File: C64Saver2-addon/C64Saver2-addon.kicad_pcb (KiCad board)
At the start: 2 copper layers, 45.7 x 35.6 mm, 25 parts, among them J1 Conn_01x12_Female, J2 Conn_01x07_Female, J3 OLED_128x32_Conn_01x04_Male, SW1 SW_Push, SW2 SW_Push, U1 INA219xIDR-SOIC, U2 ISO1541D, U3 ProMicro, U4 4N25, U5 4N25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

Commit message: revision on addon board
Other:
- board text added: "Rev 2.0"
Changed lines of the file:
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@@
     (links 78)
     (no_connects 0)
-    (area 128.06357 76.024761 194.54 122.095239)
+    (area 138.354999 81.204999 184.225001 116.915001)
     (thickness 1.6)
-    (drawings 7)
+    (drawings 9)
     (tracks 372)
     (zones 0)
@@
     (descr "Through hole straight pin header, 1x12, 2.54mm pitch, single row")
     (tags "Through hole pin header THT 1x12 2.54mm single row")
-    (fp_text reference J1 (at 0 30.48 180) (layer F.SilkS)
+    (fp_text reference J1 (at -2.0828 4.8768 180) (layer F.SilkS)
       (effects (font (size 1 1) (thickness 0.15)))
     )
@@
     )
   )
+  (gr_text "Rev 2.0" (at 180.721 84.0232) (layer F.SilkS)
+    (effects (font (size 1.1 1.1) (thickness 0.275)))
+  )
+  (gr_text "C64 Saver\nAddon\nBWACK 2018" (at 175.4378 109.4486) (layer B.SilkS)
+    (effects (font (size 1.25 1.25) (thickness 0.3)) (justify mirror))
+  )
   (gr_text OLED (at 140.335 87.63 90) (layer F.SilkS)

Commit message: saver 2.0beta - addon 1.0beta
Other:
- board text added: "Rev 2.0beta"
- board text removed: "Rev 2.0"
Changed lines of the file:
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@@
     (links 78)
     (no_connects 0)
-    (area 138.354999 81.204999 184.225001 116.915001)
+    (area 128.06357 76.024761 194.54 122.095239)
     (thickness 1.6)
     (drawings 9)
@@
     )
   )
-  (gr_text "Rev 2.0" (at 180.721 84.0232) (layer F.SilkS)
+  (gr_text "Rev 2.0beta" (at 175.26 106.68) (layer F.SilkS)
     (effects (font (size 1.1 1.1) (thickness 0.275)))
   )

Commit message: eddited schematic of addon board
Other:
- board text added: "C64 Saver Addon 1.0 BWACK 2018"
- board text removed: "Rev 2.0beta"
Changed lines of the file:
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@@
     (area 128.06357 76.024761 194.54 122.095239)
     (thickness 1.6)
-    (drawings 9)
+    (drawings 8)
     (tracks 372)
     (zones 0)
@@
     )
   )
-  (gr_text "Rev 2.0beta" (at 175.26 106.68) (layer F.SilkS)
-    (effects (font (size 1.1 1.1) (thickness 0.275)))
-  )
-  (gr_text "C64 Saver\nAddon\nBWACK 2018" (at 175.4378 109.4486) (layer B.SilkS)
+  (gr_text "C64 Saver\nAddon 1.0\nBWACK 2018" (at 175.4378 109.4486) (layer B.SilkS)
     (effects (font (size 1.25 1.25) (thickness 0.3)) (justify mirror))
   )

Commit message: SOP4 model
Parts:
- added R10: 560, Resistors_SMD:R_0603_HandSoldering, F.Cu at (178.0, 106.7)
- added R11: 560, Resistors_SMD:R_0603_HandSoldering, F.Cu at (178.0, 110.5)
- added R9: 560, Resistors_SMD:R_0603_HandSoldering, F.Cu at (172.9, 106.7)
- added U7: AP1117-50, TO_SOT_Packages_SMD:SOT-223-3_TabPin2, F.Cu at (159.0, 98.8)
- D1: footprint Diodes_SMD:D_1206 -> Diodes_SMD:D_SOD-123
- R2: footprint Resistors_SMD:R_2816_HandSoldering -> Resistors_SMD:R_2010_HandSoldering
- moved C1 21.6 mm to (163.1, 106.7), turned to 180 degrees
- moved R1 11.6 mm to (172.9, 93.3)
- moved D1 7.65 mm to (141.3, 114.3)
- moved U4 7.44 mm to (157.7, 92.4)
- moved U5 7.10 mm to (162.7, 92.4)
- moved SW2 5.72 mm to (147.3, 110.5)
- moved SW1 5.56 mm to (157.6, 110.5)
- moved R3 3.07 mm to (153.7, 92.5), turned to 270 degrees
- moved R2 1.91 mm to (158.5, 87.6)
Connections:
- C1 pad 1: 9VAC2 -> GND
- C1 pad 2: /9VRAW -> Net-(C1-Pad2)
- C4 pad 2: +5V -> Net-(C4-Pad2)
- C5 pad 1: Net-(C5-Pad1) -> /9VAC1+
- C5 pad 2: /SENSE_VAC -> Net-(C5-Pad2)
- D1 pad 1: /9VRAW -> Net-(C1-Pad2)
- D1 pad 2: /9VAC1- -> /9VAC1+
- J1 pad 1: /VIN+ -> GND2
- J2 pad 1: GND2 -> /9VAC1+
- J2 pad 2: GND2 -> /9VAC1+
- J2 pad 3: /9VAC1+ -> /9VAC1-
- J2 pad 5: 9VAC2 -> GND
- R7 pad 1: GND -> /SDA2
- R7 pad 2: Net-(C5-Pad1) -> Net-(R7-Pad2)
- R8 pad 1: Net-(C5-Pad1) -> /SENSE_VAC
- R8 pad 2: /9VAC1- -> Net-(C5-Pad2)
- U1 pad 3: /SDA2 -> /SCL2
- U1 pad 4: /SCL2 -> /SDA2
- U3 pad 23: 9VAC2 -> GND
- U3 pad 24: /9VRAW -> (no net)
- U6 pad 8: +5V -> Net-(C4-Pad2)
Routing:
- net GND: track 113.5 -> 0.00 mm
- net +5V: track 77.6 -> 0.00 mm, vias 2 -> 0
- net VIN-: track 59.5 -> 0.00 mm, vias 2 -> 0
- net /SDA1: track 56.4 -> 0.00 mm, vias 1 -> 0
- net GND2: track 55.8 -> 0.00 mm
- net /9VAC1-: track 54.2 -> 0.00 mm, vias 2 -> 0
- net /SCL1: track 47.0 -> 0.00 mm, vias 2 -> 0
- net Net-(C3-Pad2): track 44.1 -> 0.00 mm
- net /VIN+: track 43.8 -> 0.00 mm
- net Net-(SW2-Pad2): track 40.3 -> 0.00 mm
- net /9VRAW: track 38.0 -> 0.00 mm, vias 1 -> 0
- net Net-(SW1-Pad2): track 29.1 -> 0.00 mm
- net 9VAC2: track 27.7 -> 0.00 mm
- net /9VAC1+: track 23.6 -> 0.00 mm, vias 1 -> 0
- net /SENSE_ACCUR: track 20.7 -> 0.00 mm, vias 1 -> 0
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
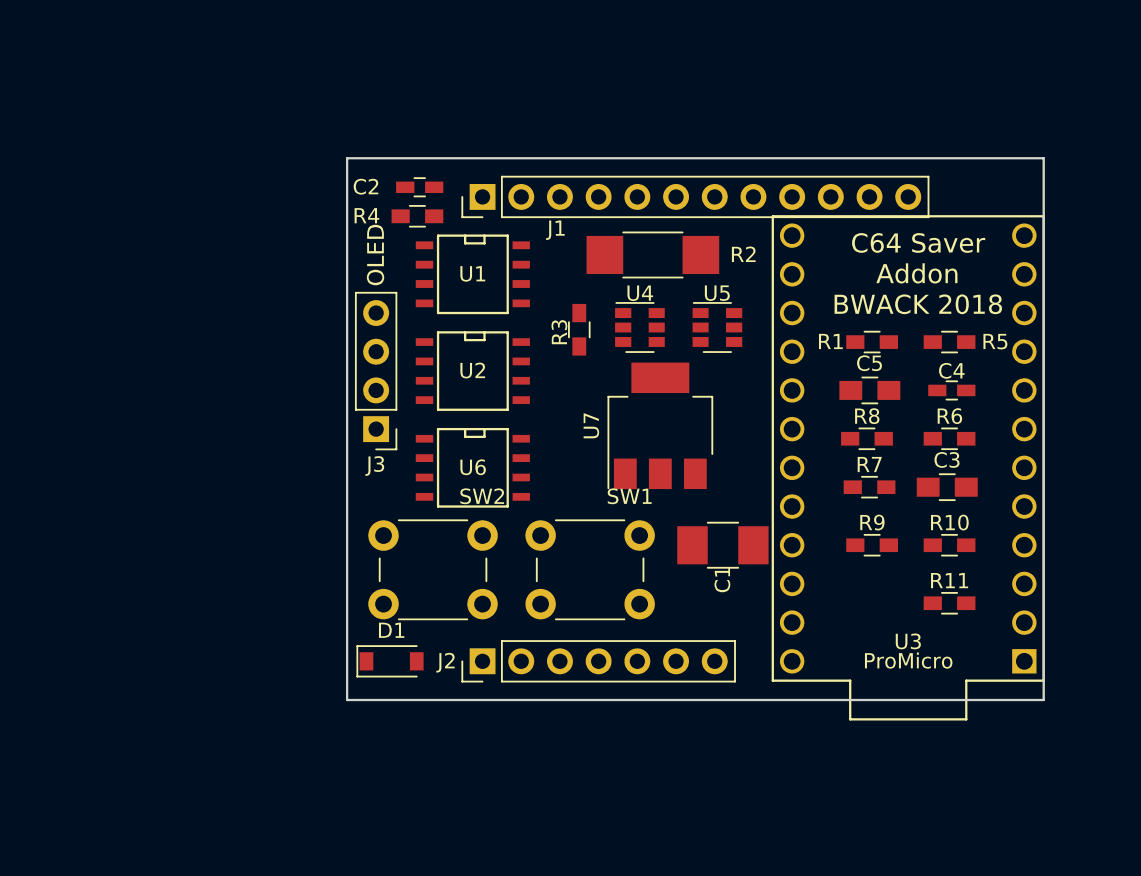
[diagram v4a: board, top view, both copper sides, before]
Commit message: ssop. 0603 capacitors
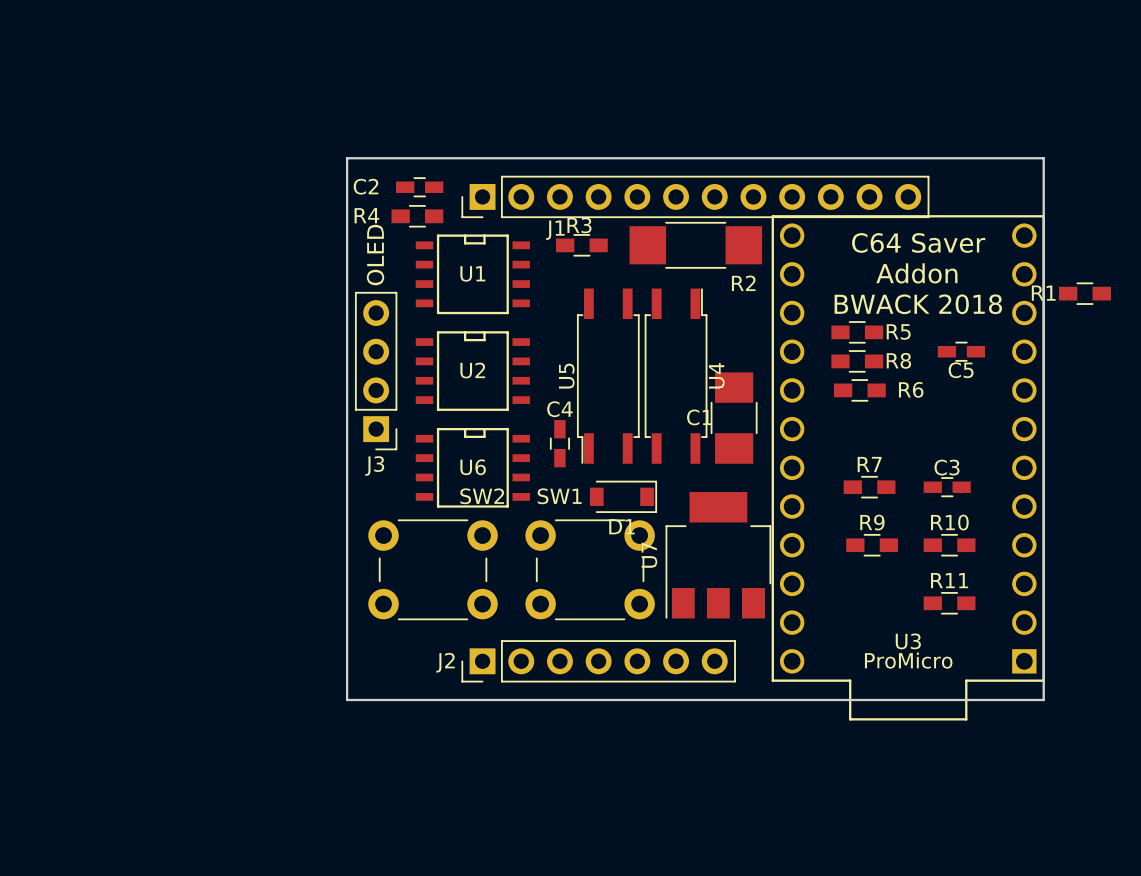
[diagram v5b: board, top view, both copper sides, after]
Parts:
- C3, C5: footprint Capacitors_SMD:C_0805_HandSoldering -> Capacitors_SMD:C_0603_HandSoldering
- U4, U5: value 4N25 -> TLP291; footprint TO_SOT_Packages_SMD:SOT-23-6 -> Housings_SOIC:SO-4_7.6x3.6mm_Pitch2.54mm
- moved C4 26.0 mm to (152.4, 100.0), turned to 90 degrees
- moved D1 18.6 mm to (156.5, 103.5), turned to 180 degrees
- moved R1 14.3 mm to (186.9, 90.2)
- moved U7 9.31 mm to (162.8, 107.3)
- moved C1 8.38 mm to (163.8, 98.3), turned to 90 degrees
- moved U5 7.83 mm to (155.6, 95.6), turned to 90 degrees
- moved R6 6.69 mm to (172.1, 96.5), turned to 180 degrees
- moved C5 6.52 mm to (178.8, 94.0), turned to 180 degrees
- moved R5 6.09 mm to (171.9, 92.7)
- moved R3 5.55 mm to (153.8, 87.0), turned to 180 degrees
- moved R8 5.12 mm to (171.9, 94.6)
- moved U4 3.97 mm to (160.0, 95.6), turned to 270 degrees
- moved R2 2.89 mm to (161.3, 87.0)
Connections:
- U4 pad 1: Net-(R3-Pad1) -> VIN-
- U4 pad 2: OVERVOLTAGE -> PGATE
- U4 pad 3: (no net) -> GND
- U4 pad 4: GND -> /HOLD
- U5 pad 1: /HOLD -> Net-(R3-Pad1)
- U5 pad 2: GND -> OVERVOLTAGE
- U5 pad 3: (no net) -> GND
- U5 pad 4: PGATE -> /#OVERVOLTAGE

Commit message: fit to hammond1591, larger board.
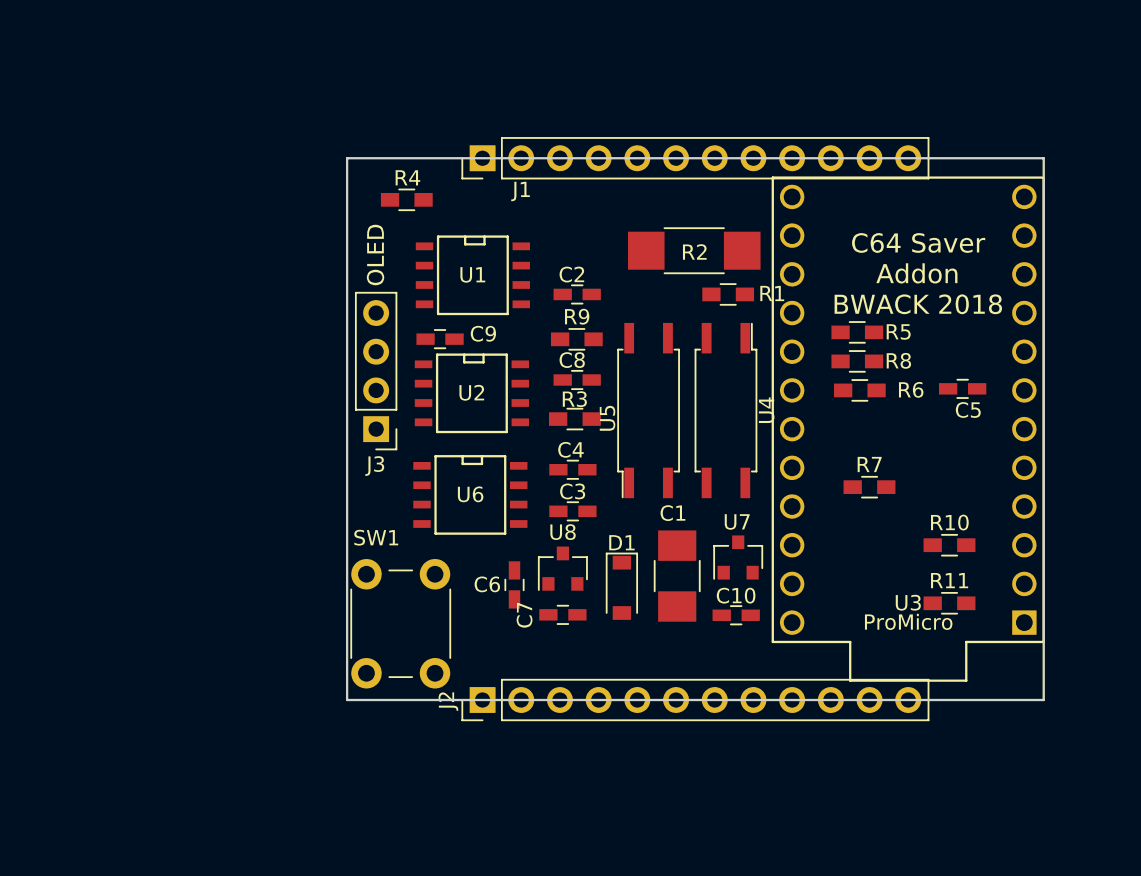
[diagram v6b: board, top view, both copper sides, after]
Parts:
- removed SW2: SW_Push, Buttons_Switches_THT:SW_PUSH_6mm_h13mm
- added C10: 1u, Capacitors_SMD:C_0603_HandSoldering, F.Cu at (164.0, 111.3)
- added C6: 1u, Capacitors_SMD:C_0603_HandSoldering, F.Cu at (149.4, 109.3)
- added C7: 1u, Capacitors_SMD:C_0603_HandSoldering, F.Cu at (152.6, 111.3)
- added C8: 100n, Capacitors_SMD:C_0603_HandSoldering, F.Cu at (153.5, 95.8)
- added C9: 100n, Capacitors_SMD:C_0603_HandSoldering, F.Cu at (144.5, 93.2)
- added REF**: hammond1591XXLGY_pcb, hammond1591:hammond1591XXLGY_pcb, F.Cu at (121.5, 125.1)
- added U8: MCP1700-5002E_SOT23, TO_SOT_Packages_SMD:SOT-23, F.Cu at (152.6, 108.2)
- J2: value Conn_01x07_Female -> Conn_01x12_Female; footprint Pin_Headers:Pin_Header_Straight_1x07_Pitch2.54mm -> Pin_Headers:Pin_Header_Straight_1x12_Pitch2.54mm
- U7: value AP1117-50 -> MCP1700-5002E_SOT23; footprint TO_SOT_Packages_SMD:SOT-223-3_TabPin2 -> TO_SOT_Packages_SMD:SOT-23
- moved C3 24.6 mm to (153.2, 104.5), turned to 180 degrees
- moved R9 23.6 mm to (153.5, 93.2)
- moved R1 23.4 mm to (163.4, 90.2)
- moved SW1 13.6 mm to (144.2, 108.6), turned to 270 degrees
- moved C2 12.5 mm to (153.5, 90.2), turned to 0 degrees
- moved R3 11.4 mm to (153.4, 98.4)
- moved C1 11.0 mm to (160.1, 108.7)
- moved D1 5.97 mm to (156.5, 109.5), turned to 270 degrees
- moved U4 3.98 mm to (163.3, 97.8)
- moved U5 3.48 mm to (158.2, 97.8)
- moved J2 2.54 mm to (147.3, 116.8)
- moved J1 2.54 mm to (147.3, 81.3)
- moved U3 2.54 mm to (175.3, 97.8)
- moved C5 2.44 mm to (178.8, 96.4)
- moved C4 1.91 mm to (153.2, 101.7), turned to 180 degrees
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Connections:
- net GND2 renamed GNDD
- C2 pad 1: /VIN+ -> /VDD2
- R10 pad 1: /SCL1 -> /SDA1
- R10 pad 2: Net-(R10-Pad2) -> +5V
- R11 pad 1: /SDA1 -> /SCL1
- R11 pad 2: Net-(R10-Pad2) -> +5V
- R7 pad 2: Net-(R7-Pad2) -> /VDD2
- R9 pad 2: Net-(R7-Pad2) -> /VDD2
- U1 pad 5: /VIN+ -> /VDD2
- U2 pad 8: VIN- -> /VDD2
- U3 pad 1: (no net) -> Net-(U3-Pad1)
- U3 pad 10: (no net) -> Net-(U3-Pad10)
- U3 pad 11: (no net) -> Net-(U3-Pad11)
- U3 pad 12: (no net) -> Net-(U3-Pad12)
- U3 pad 15: (no net) -> Net-(U3-Pad15)
- U3 pad 16: (no net) -> Net-(U3-Pad16)
- U3 pad 19: (no net) -> Net-(U3-Pad19)
- U3 pad 2: (no net) -> Net-(U3-Pad2)
- U3 pad 20: (no net) -> Net-(U3-Pad20)
- U3 pad 22: (no net) -> Net-(U3-Pad22)
- U3 pad 24: (no net) -> Net-(U3-Pad24)
- U3 pad 9: (no net) -> Net-(U3-Pad9)
- U4 pad 1: VIN- -> /HOLD
- U4 pad 2: PGATE -> GND
- U4 pad 3: GND -> PGATE
- U4 pad 4: /HOLD -> VIN-

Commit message: hammond1551G. It will be a tight fit !
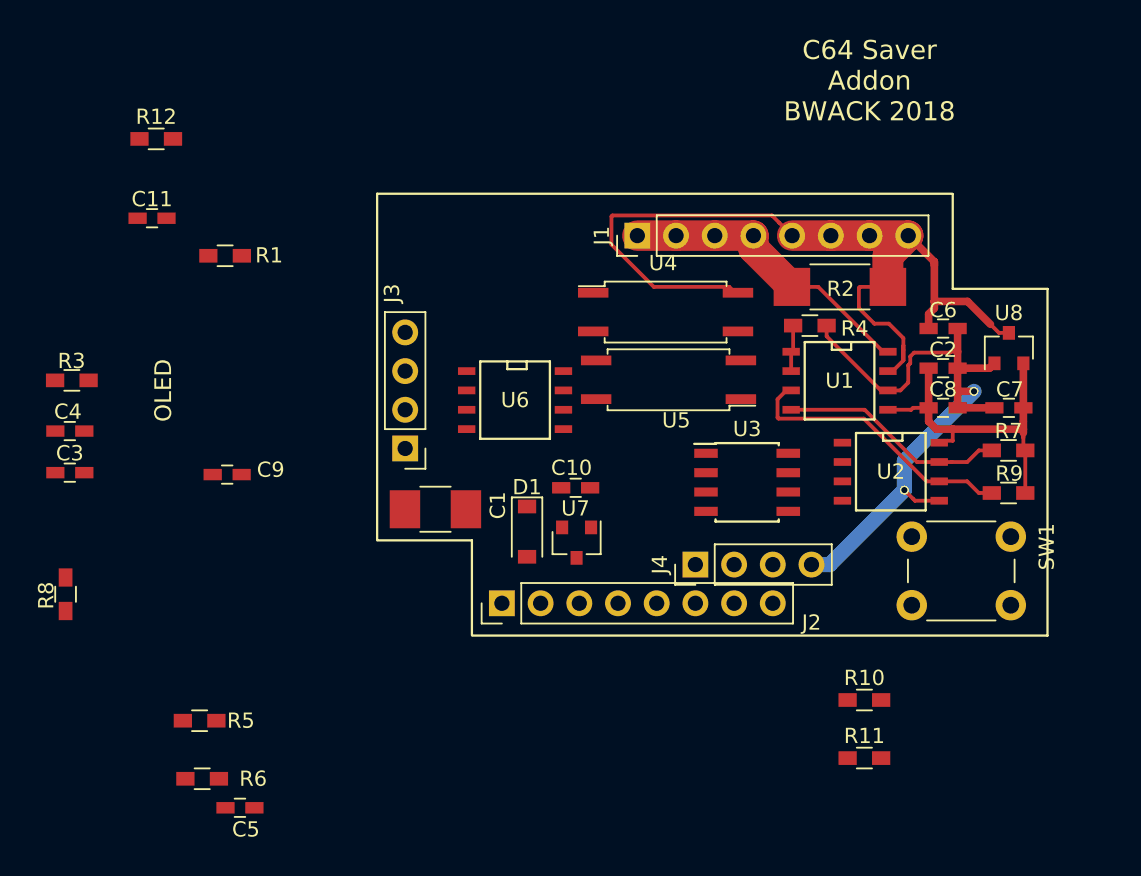
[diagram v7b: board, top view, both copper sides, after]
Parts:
- removed the REF** at (121.5, 125.1)
- added C11: 100n, Capacitors_SMD:C_0603_HandSoldering, F.Cu at (125.6, 85.2)
- added J4: Conn_01x04_Female, Pin_Headers:Pin_Header_Straight_1x04_Pitch2.54mm, F.Cu at (161.3, 108.0)
- added R12: 470, Resistors_SMD:R_0603_HandSoldering, F.Cu at (125.9, 80.0)
- added REF**: HAMMOND_1551G, HAMMOND:HAMMOND_1551G, F.Cu at (152.4, 86.4)
- C5: value 1u -> 100n
- J1, J2: value Conn_01x12_Female -> Conn_01x08_Female; footprint Pin_Headers:Pin_Header_Straight_1x12_Pitch2.54mm -> Pin_Headers:Pin_Header_Straight_1x08_Pitch2.54mm
- R5, R6: value 560 -> 470k
- R8: value 560 -> 4k7
- U3: value ProMicro -> ATTINY85-20SU; footprint promicro:ProMicro -> Housings_SOIC:SOIC-8_3.9x4.9mm_Pitch1.27mm
- moved C5 54.8 mm to (131.4, 123.9)
- moved R8 54.2 mm to (120.0, 109.9), turned to 90 degrees
- moved R6 50.1 mm to (128.9, 122.0)
- moved R5 50.1 mm to (128.7, 118.2)
- moved SW1 37.8 mm to (182.0, 110.6), turned to 180 degrees
- moved C3 33.1 mm to (120.2, 101.9)
- moved C4 33.1 mm to (120.2, 99.2)
- moved R1 33.1 mm to (130.4, 87.7)
- moved R3 33.1 mm to (120.4, 95.9)
- moved C6 32.8 mm to (177.5, 92.5), turned to 180 degrees
- moved U8 32.7 mm to (181.9, 93.7)
- moved C7 32.3 mm to (181.9, 97.7)
- moved R9 30.1 mm to (181.8, 103.3)
- moved U2 28.0 mm to (174.1, 101.9)
- moved R4 27.7 mm to (168.8, 92.3)
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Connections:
- C5 pad 1: /9VAC1+ -> Net-(C5-Pad1)
- C5 pad 2: Net-(C5-Pad2) -> /SENSE_VAC
- J1 pad 1: GNDD -> /VIN+
- J1 pad 5: /VIN+ -> VIN-
- J1 pad 6: /VIN+ -> VIN-
- J2 pad 3: /9VAC1- -> /9VAC1+
- J2 pad 4: /9VAC1- -> /9VAC1+
- J2 pad 5: GND -> /9VAC1-
- J2 pad 6: OVERVOLTAGE -> /9VAC1-
- J2 pad 7: PGATE -> /9VAC1-
- J2 pad 8: Net-(J2-Pad8) -> /9VAC1-
- R1 pad 1: /HOLD -> /HOLD_
- R1 pad 2: Net-(R1-Pad2) -> /HOLD
- R8 pad 1: /SENSE_VAC -> Net-(C5-Pad1)
- R8 pad 2: Net-(C5-Pad2) -> /9VAC1+
- SW1 pad 2: Net-(SW1-Pad2) -> /SENSE_VAC
- U3 pad 1: Net-(U3-Pad1) -> /#OVERVOLTAGE
- U3 pad 2: Net-(U3-Pad2) -> /SENSE_ACCUR
- U3 pad 3: GND -> /HOLD_
- U3 pad 6: /SCL1 -> /SENSE_VAC
- U3 pad 7: Net-(SW1-Pad2) -> /SCL1
- U3 pad 8: Net-(U3-Pad8) -> +5V
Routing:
- net VIN-: track 0.00 -> 64.1 mm
- net GNDD: track 0.00 -> 43.5 mm, vias 0 -> 2
- net /VDD2: track 0.00 -> 22.8 mm
- net /VIN+: track 0.00 -> 20.1 mm
- net /SCL2: track 0.00 -> 18.5 mm
- net /SDA2: track 0.00 -> 14.9 mm
- net Net-(R4-Pad2): track 0.00 -> 3.04 mm
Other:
- board outline removed
- board text removed: "C64 Saver Addon 1.0 BWACK 2018"

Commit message: addon board component placement done. layout begun.
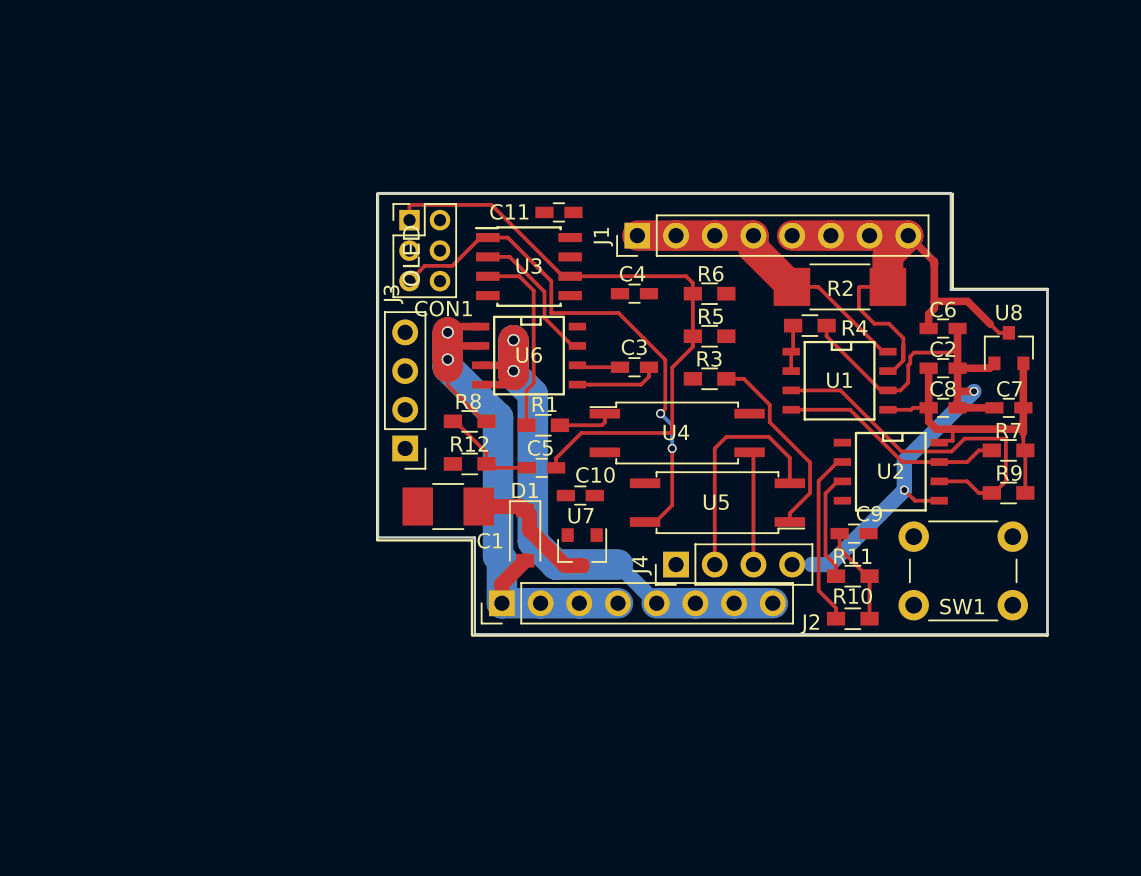
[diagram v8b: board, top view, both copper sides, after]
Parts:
- added CON1: AVR-ISP-6, Pin_Headers:Pin_Header_Straight_2x03_Pitch2.00mm, F.Cu at (142.5, 85.3)
- moved R6 46.1 mm to (162.2, 90.2)
- moved R5 41.9 mm to (162.2, 93.0)
- moved R3 41.9 mm to (162.2, 95.8)
- moved C9 41.3 mm to (171.7, 105.9)
- moved C4 38.1 mm to (157.3, 90.2)
- moved C3 37.7 mm to (157.3, 95.0)
- moved C5 29.8 mm to (151.2, 101.6), turned to 0 degrees
- moved R12 29.6 mm to (146.5, 101.3)
- moved R8 28.8 mm to (146.5, 98.6), turned to 0 degrees
- moved C11 26.7 mm to (152.3, 84.8)
- moved R1 23.7 mm to (151.3, 98.8)
- moved U3 20.1 mm to (150.4, 88.4)
- moved R11 12.0 mm to (171.6, 108.7)
- moved U5 8.68 mm to (162.7, 103.9)
- moved U4 7.97 mm to (160.1, 99.3)
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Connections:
- net Net-(C3-Pad2) renamed /FILTER
- C4 pad 2: Net-(C4-Pad2) -> +5V
- U6 pad 8: Net-(C4-Pad2) -> +5V
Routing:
- net /9VAC1+: track 0.00 -> 44.4 mm, vias 0 -> 2
- net /SENSE_VAC: track 0.00 -> 41.0 mm
- net /9VAC1-: track 0.00 -> 38.4 mm, vias 0 -> 2
- net /#OVERVOLTAGE: track 0.00 -> 34.7 mm, vias 0 -> 2
- net VIN-: track 64.1 -> 40.3 mm
- net OVERVOLTAGE: track 0.00 -> 15.1 mm
- net Net-(R3-Pad1): track 0.00 -> 12.9 mm
- net /HOLD_: track 0.00 -> 12.4 mm
- net /SDA1: track 0.00 -> 11.6 mm
- net /SENSE_ACCUR: track 0.00 -> 9.30 mm
- net Net-(C1-Pad2): track 0.00 -> 8.98 mm
- net PGATE: track 0.00 -> 7.47 mm
- net /SCL1: track 0.00 -> 7.16 mm
- net +5V: track 0.00 -> 6.60 mm
- net Net-(C5-Pad1): track 0.00 -> 6.57 mm
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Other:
- board outline added: 43.9 x 29 mm
